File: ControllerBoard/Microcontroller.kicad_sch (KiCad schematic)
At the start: 22 parts, among them U3 nRF52810-QCxx, Y1 32.768kHz 12.5pF, Y2 32MHz 8pF <40ppm

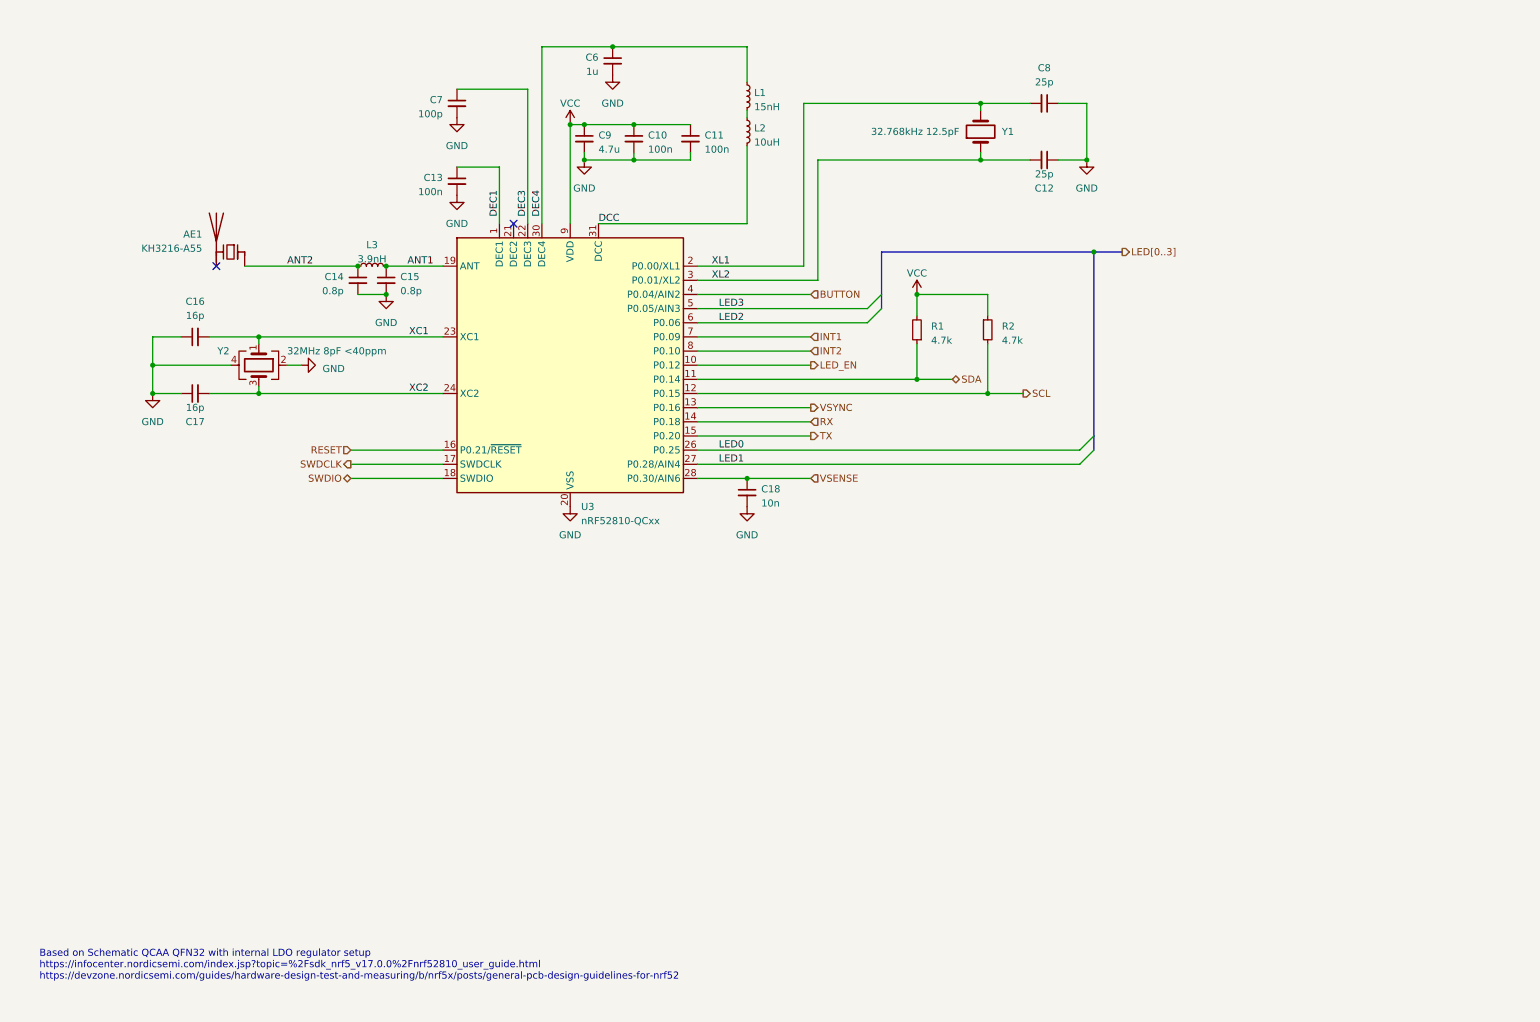
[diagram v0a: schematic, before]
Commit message: Remove LED driver
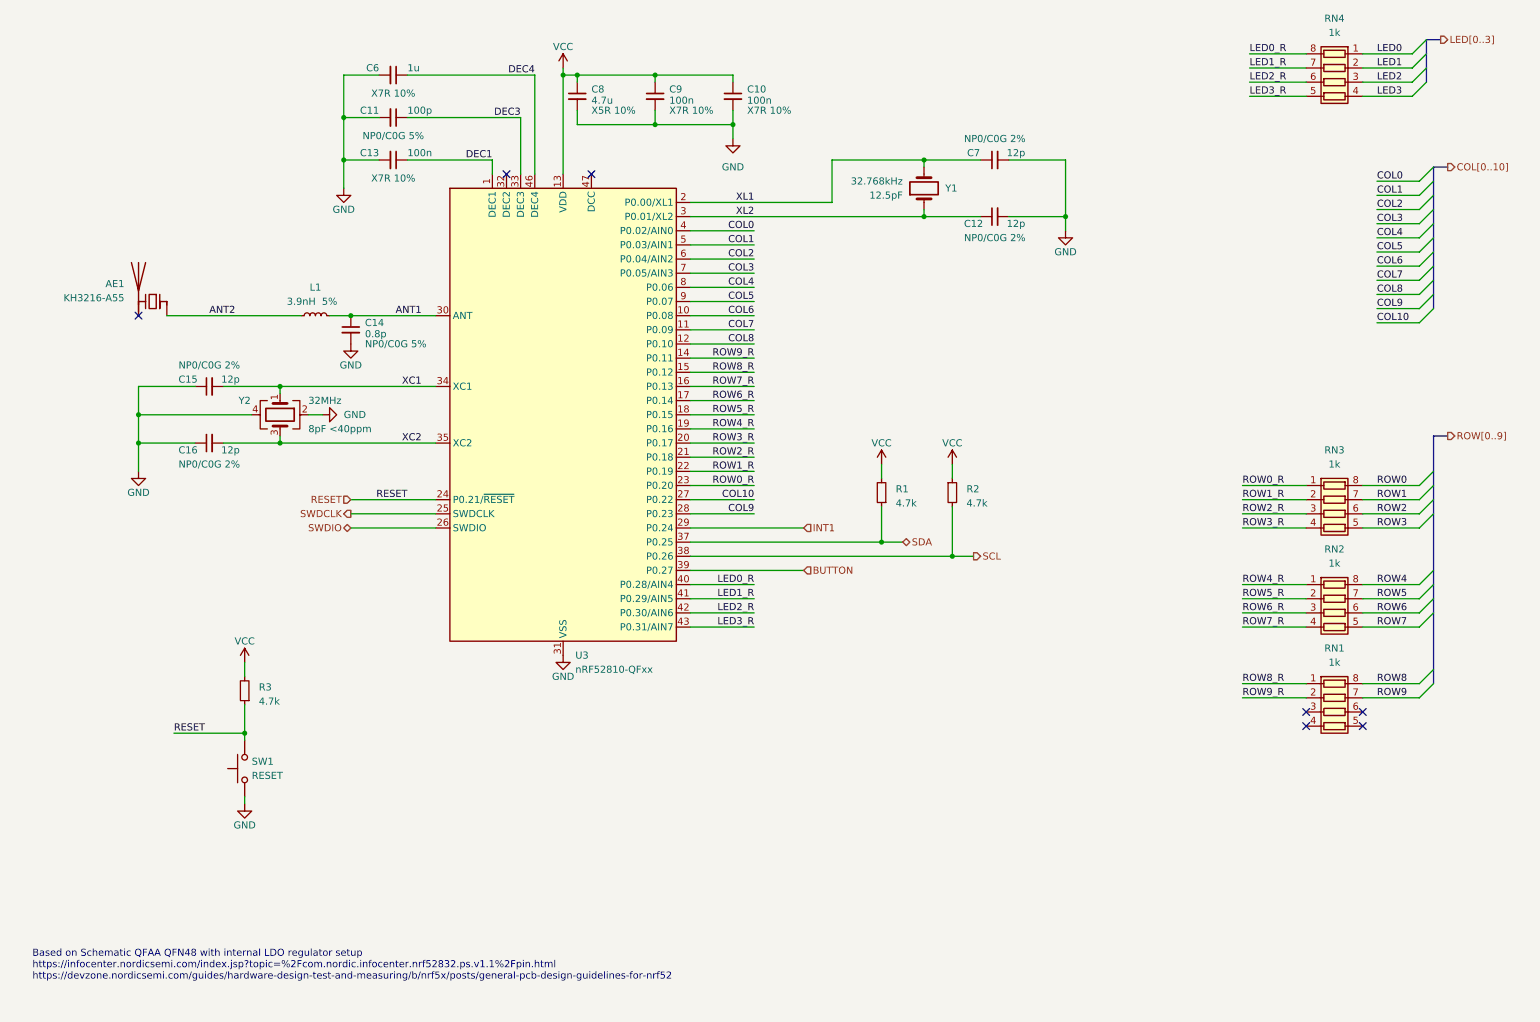
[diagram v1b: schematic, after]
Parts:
- removed C17: 16p, Capacitor_SMD:C_0402_1005Metric, symbol Device:C_Small
- removed C18: 10n, Capacitor_SMD:C_0402_1005Metric, symbol Device:C_Small
- removed L2: 10uH, Inductor_SMD:L_0603_1608Metric, symbol Device:L_Small
- removed L3: 3.9nH, Inductor_SMD:L_0402_1005Metric, symbol Device:L_Small
- removed U3: nRF52810-QCxx, Package_DFN_QFN:QFN-32-1EP_5x5mm_P0.5mm_EP3.6x3.6mm, symbol MCU_Nordic:nRF52810-QCxx
- added R3: 4.7k, Resistor_SMD:R_0402_1005Metric, symbol Device:R_Small
- added RN1, RN2, RN3, RN4: 1k, Resistor_SMD:R_Array_Concave_4x0402, symbol Device:R_Pack04
- added SW1: RESET, Button_Switch_SMD:SW_Push_SPST_NO_Alps_SKRK, symbol Switch:SW_Push
- added U3: nRF52810-QFxx, Package_DFN_QFN:QFN-48-1EP_6x6mm_P0.4mm_EP4.6x4.6mm, symbol MCU_Nordic:nRF52810-QFxx
- C11: value 100n -> 100p
- C12: value 25p -> 12p
- C15: value 0.8p -> 12p
- C16: value 16p -> 12p
- C6: footprint Capacitor_SMD:C_0402_1005Metric -> Capacitor_SMD:C_0603_1608Metric
- C7: value 100p -> 12p
- C8: value 25p -> 4.7u; footprint Capacitor_SMD:C_0402_1005Metric -> Capacitor_SMD:C_0603_1608Metric
- C9: value 4.7u -> 100n; footprint Capacitor_SMD:C_0603_1608Metric -> Capacitor_SMD:C_0402_1005Metric
- L1: value 15nH -> 3.9nH
- Y1: value 32.768kHz 12.5pF -> 32.768kHz
- Y2: value 32MHz 8pF <40ppm -> 32MHz
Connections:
- net ANT1: now also C14.1, L1.2, U3.30 (ANT); no longer C15.1
- net ANT2: now also L1.1; no longer C14.1
- net BUTTON: now also U3.39 (P0.27)
- net DEC1: now also U3.1 (DEC1)
- net DEC3: now also C11.1, U3.33 (DEC3); no longer C7.1
- net DEC4: now also U3.46 (DEC4); no longer L1.1
- net GND: now also C12.2, C15.1, C8.2, SW1.1, U3.31 (VSS), U3.45 (VSS), U3.49 (VSS); no longer C12.1, C15.2, C8.1
- net INT1: now also U3.29 (P0.24)
- net LED0: now also RN4.1 (R1.1)
- net LED1: now also RN4.2 (R2.1)
- net LED2: now also RN4.3 (R3.1)
- net LED3: now also RN4.4 (R4.1)
- net RESET: now also R3.1, SW1.2, U3.24 (P0.21/~{RESET})
- net SCL: now also U3.38 (P0.26)
- net SDA: now also U3.37 (P0.25)
- net SWDCLK: now also U3.25 (SWDCLK)
- net SWDIO: now also U3.26 (SWDIO)
- net VCC: now also C8.1, R3.2, U3.13 (VDD), U3.36 (VDD), U3.48 (VDD); no longer C11.1
- net XC1: now also C15.2, U3.34 (XC1); no longer C16.2
- net XC2: now also C16.2, U3.35 (XC2)
- net XL1: now also C7.1, U3.2 (P0.00/XL1); no longer C8.2
- net XL2: now also C12.1, U3.3 (P0.01/XL2); no longer C12.2
- new net COL0: U3.4 (P0.02/AIN0)
- new net COL1: U3.5 (P0.03/AIN1)
- new net COL10: U3.27 (P0.22)
- new net COL2: U3.6 (P0.04/AIN2)
- new net COL3: U3.7 (P0.05/AIN3)
- new net COL4: U3.8 (P0.06)
- new net COL5: U3.9 (P0.07)
- new net COL6: U3.10 (P0.08)
- new net COL7: U3.11 (P0.09)
- new net COL8: U3.12 (P0.10)
- new net COL9: U3.28 (P0.23)
- new net LED0_R: RN4.8 (R1.2), U3.40 (P0.28/AIN4)
- new net LED1_R: RN4.7 (R2.2), U3.41 (P0.29/AIN5)
- new net LED2_R: RN4.6 (R3.2), U3.42 (P0.30/AIN6)
- new net LED3_R: RN4.5 (R4.2), U3.43 (P0.31/AIN7)
- new net ROW0: RN3.8 (R1.2)
- new net ROW0_R: RN3.1 (R1.1), U3.23 (P0.20)
- new net ROW1: RN3.7 (R2.2)
- new net ROW1_R: RN3.2 (R2.1), U3.22 (P0.19)
- new net ROW2: RN3.6 (R3.2)
- new net ROW2_R: RN3.3 (R3.1), U3.21 (P0.18)
- new net ROW3: RN3.5 (R4.2)
- new net ROW3_R: RN3.4 (R4.1), U3.20 (P0.17)
- new net ROW4: RN2.8 (R1.2)
- new net ROW4_R: RN2.1 (R1.1), U3.19 (P0.16)
- new net ROW5: RN2.7 (R2.2)
- new net ROW5_R: RN2.2 (R2.1), U3.18 (P0.15)
- new net ROW6: RN2.6 (R3.2)
- new net ROW6_R: RN2.3 (R3.1), U3.17 (P0.14)
- new net ROW7: RN2.5 (R4.2)
- new net ROW7_R: RN2.4 (R4.1), U3.16 (P0.13)
- new net ROW8: RN1.8 (R1.2)
- new net ROW8_R: RN1.1 (R1.1), U3.15 (P0.12)
- new net ROW9: RN1.7 (R2.2)
- new net ROW9_R: RN1.2 (R2.1), U3.14 (P0.11)
- no-connect marks 2 -> 7
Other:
- note added: "Based on Schematic QFAA QFN48 with internal LDO regulator setup https://infocenter.nordicsemi.com/index.jsp?topic=%2Fcom.nordic.infocenter.nrf52832.ps.v1.1%2Fpin.html https://devzone.nordicsemi.com/guides/hardware-design-test-and-measuring/b/nrf5x/posts/general-pcb-design-guidelines-for-nrf52"
- note removed: "Based on Schematic QCAA QFN32 with internal LDO regulator setup https://infocenter.nordicsemi.com/index.jsp?topic=%2Fsdk_nrf5_v17.0.0%2Fnrf52810_user_guide.html https://devzone.nordicsemi.com/guides/hardware-design-test-and-measuring/b/nrf5x/posts/general-pcb-design-guidelines-for-nrf52"

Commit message: Change led matrix routing for sinking current through mcu, sourcing from battery
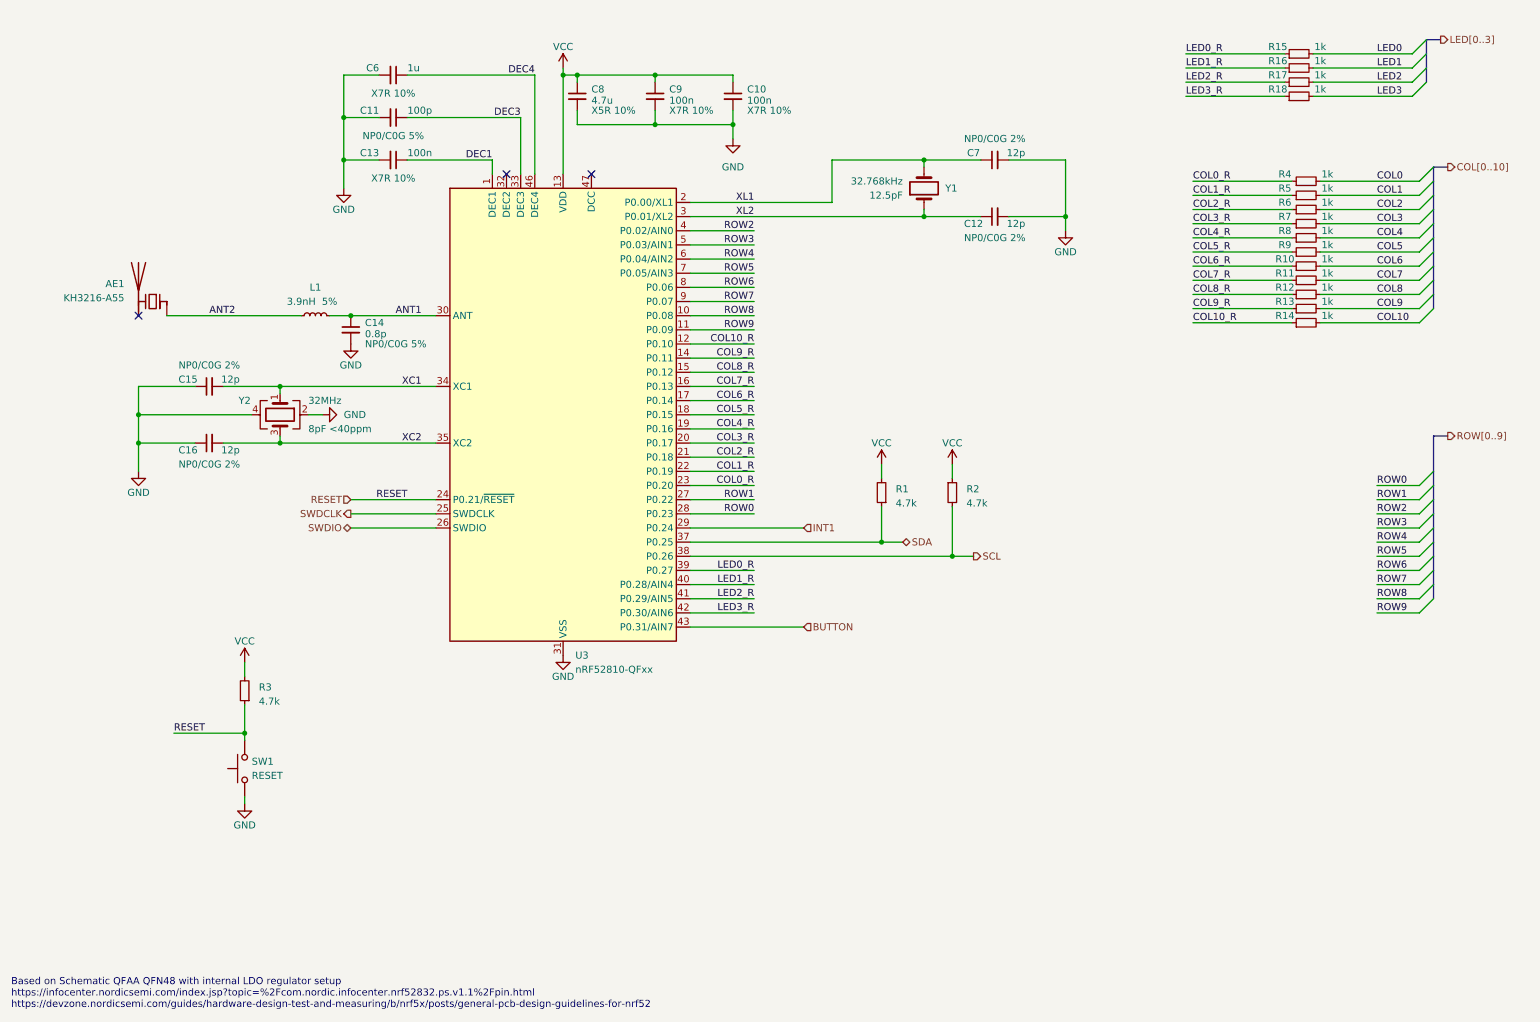
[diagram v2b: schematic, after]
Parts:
- removed RN1, RN2, RN3, RN4: 1k, Resistor_SMD:R_Array_Concave_4x0402, symbol Device:R_Pack04
- added R10, R11, R12, R13, R14, R15, R16, R17, R18, R4, R5, R6, R7, R8, R9: 1k, Resistor_SMD:R_0402_1005Metric, symbol Device:R_Small
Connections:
- net BUTTON: now also U3.43 (P0.31/AIN7); no longer U3.39 (P0.27)
- net COL0: now also R4.2; no longer U3.4 (P0.02/AIN0)
- net COL1: now also R5.2; no longer U3.5 (P0.03/AIN1)
- net COL10: now also R14.2; no longer U3.27 (P0.22)
- net COL2: now also R6.2; no longer U3.6 (P0.04/AIN2)
- net COL3: now also R7.2; no longer U3.7 (P0.05/AIN3)
- net COL4: now also R8.2; no longer U3.8 (P0.06)
- net COL5: now also R9.2; no longer U3.9 (P0.07)
- net COL6: now also R10.2; no longer U3.10 (P0.08)
- net COL7: now also R11.2; no longer U3.11 (P0.09)
- net COL8: now also R12.2; no longer U3.12 (P0.10)
- net COL9: now also R13.2; no longer U3.28 (P0.23)
- net LED0: now also R15.2
- net LED0_R: now also U3.39 (P0.27), R15.1; no longer U3.40 (P0.28/AIN4)
- net LED1: now also R16.2
- net LED1_R: now also U3.40 (P0.28/AIN4), R16.1; no longer U3.41 (P0.29/AIN5)
- net LED2: now also R17.2
- net LED2_R: now also U3.41 (P0.29/AIN5), R17.1; no longer U3.42 (P0.30/AIN6)
- net LED3: now also R18.2
- net LED3_R: now also U3.42 (P0.30/AIN6), R18.1; no longer U3.43 (P0.31/AIN7)
- net ROW0: now also U3.28 (P0.23)
- net ROW1: now also U3.27 (P0.22)
- net ROW2: now also U3.4 (P0.02/AIN0)
- net ROW3: now also U3.5 (P0.03/AIN1)
- net ROW4: now also U3.6 (P0.04/AIN2)
- net ROW5: now also U3.7 (P0.05/AIN3)
- net ROW6: now also U3.8 (P0.06)
- net ROW7: now also U3.9 (P0.07)
- net ROW8: now also U3.10 (P0.08)
- net ROW9: now also U3.11 (P0.09)
- net ROW0_R renamed COL0_R
- net COL0_R: now also R4.1
- net ROW1_R renamed COL1_R
- net COL1_R: now also R5.1
- net ROW2_R renamed COL2_R
- net COL2_R: now also R6.1
- net ROW3_R renamed COL3_R
- net COL3_R: now also R7.1
- net ROW4_R renamed COL4_R
- net COL4_R: now also R8.1
- net ROW5_R renamed COL5_R
- net COL5_R: now also R9.1
- net ROW6_R renamed COL6_R
- net COL6_R: now also R10.1
- net ROW7_R renamed COL7_R
- net COL7_R: now also R11.1
- net ROW8_R renamed COL8_R
- net COL8_R: now also R12.1
- net ROW9_R renamed COL9_R
- net COL9_R: now also R13.1
- new net COL10_R: R14.1, U3.12 (P0.10)
- no-connect marks 7 -> 3
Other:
- title: (none) -> WordWatch - Controller Board
